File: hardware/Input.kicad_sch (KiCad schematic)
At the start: 40 parts, among them J10 USB_C_Receptacle_USB2.0, J4 AudioJack3, J5 Conn_Coaxial, J6 Conn_Coaxial, J7 Conn_Coaxial, J8 Conn_Coaxial, J9 Barrel_Jack_Switch, U23 74LVCH2T45DC, U24 74LVCH2T45DC, U25 74LVCH2T45DC

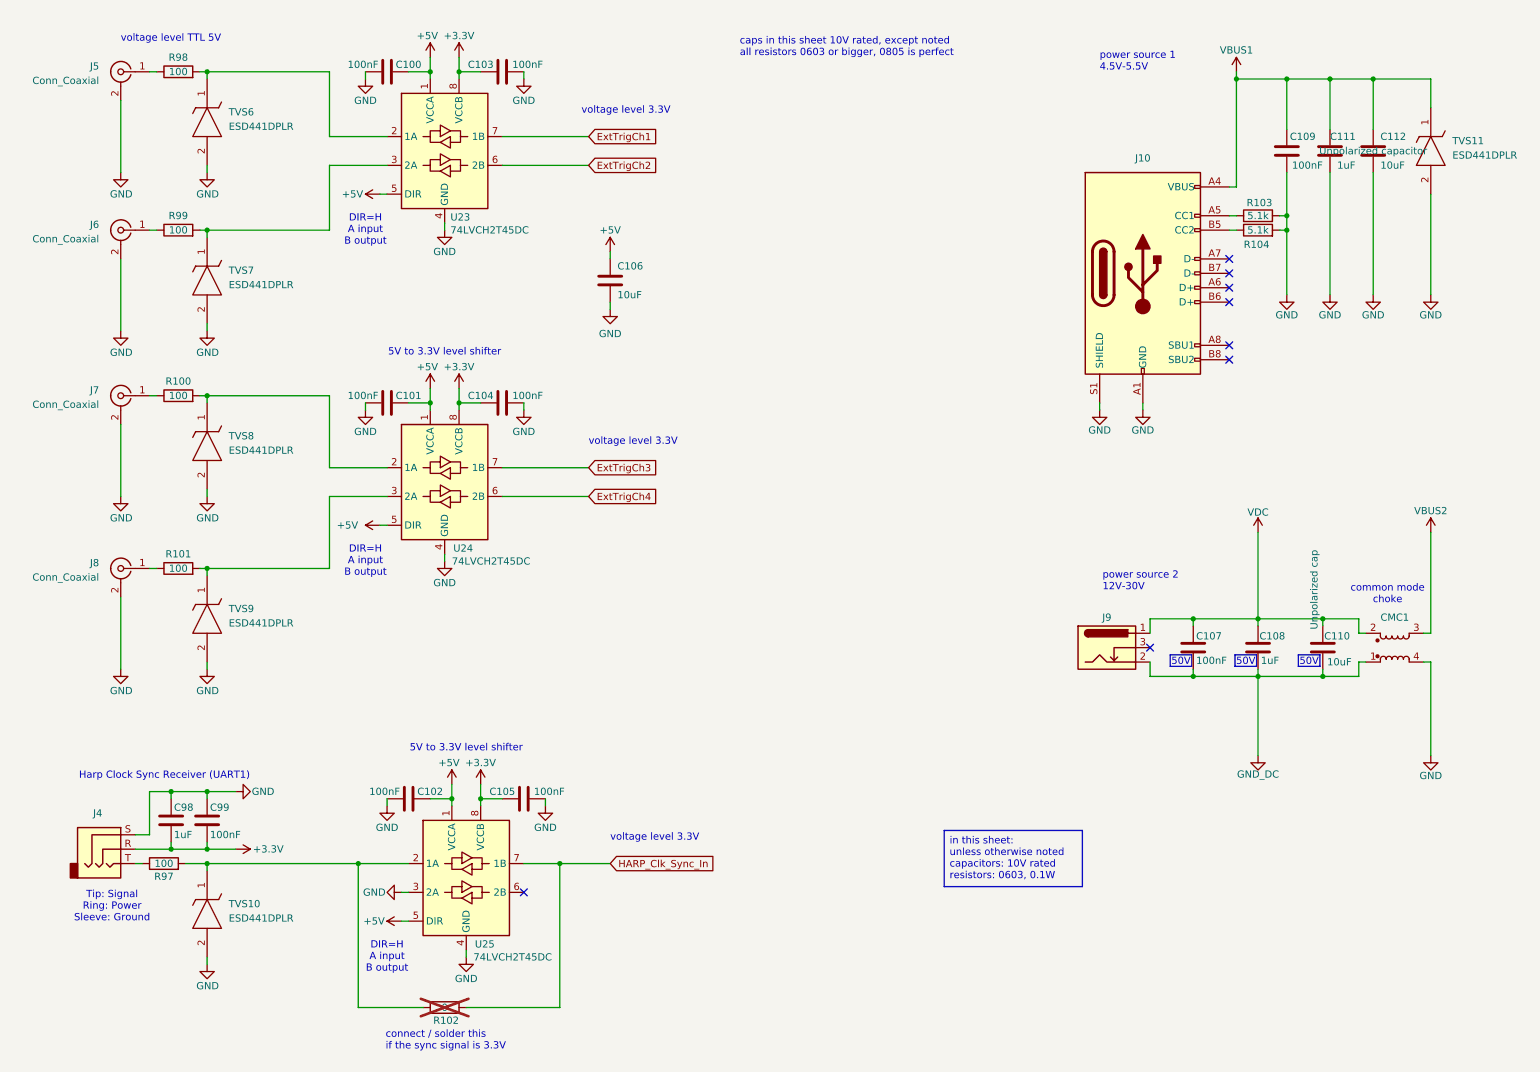
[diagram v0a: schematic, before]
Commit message: BOM for all capacitors and resistors is added correctly to the schematic
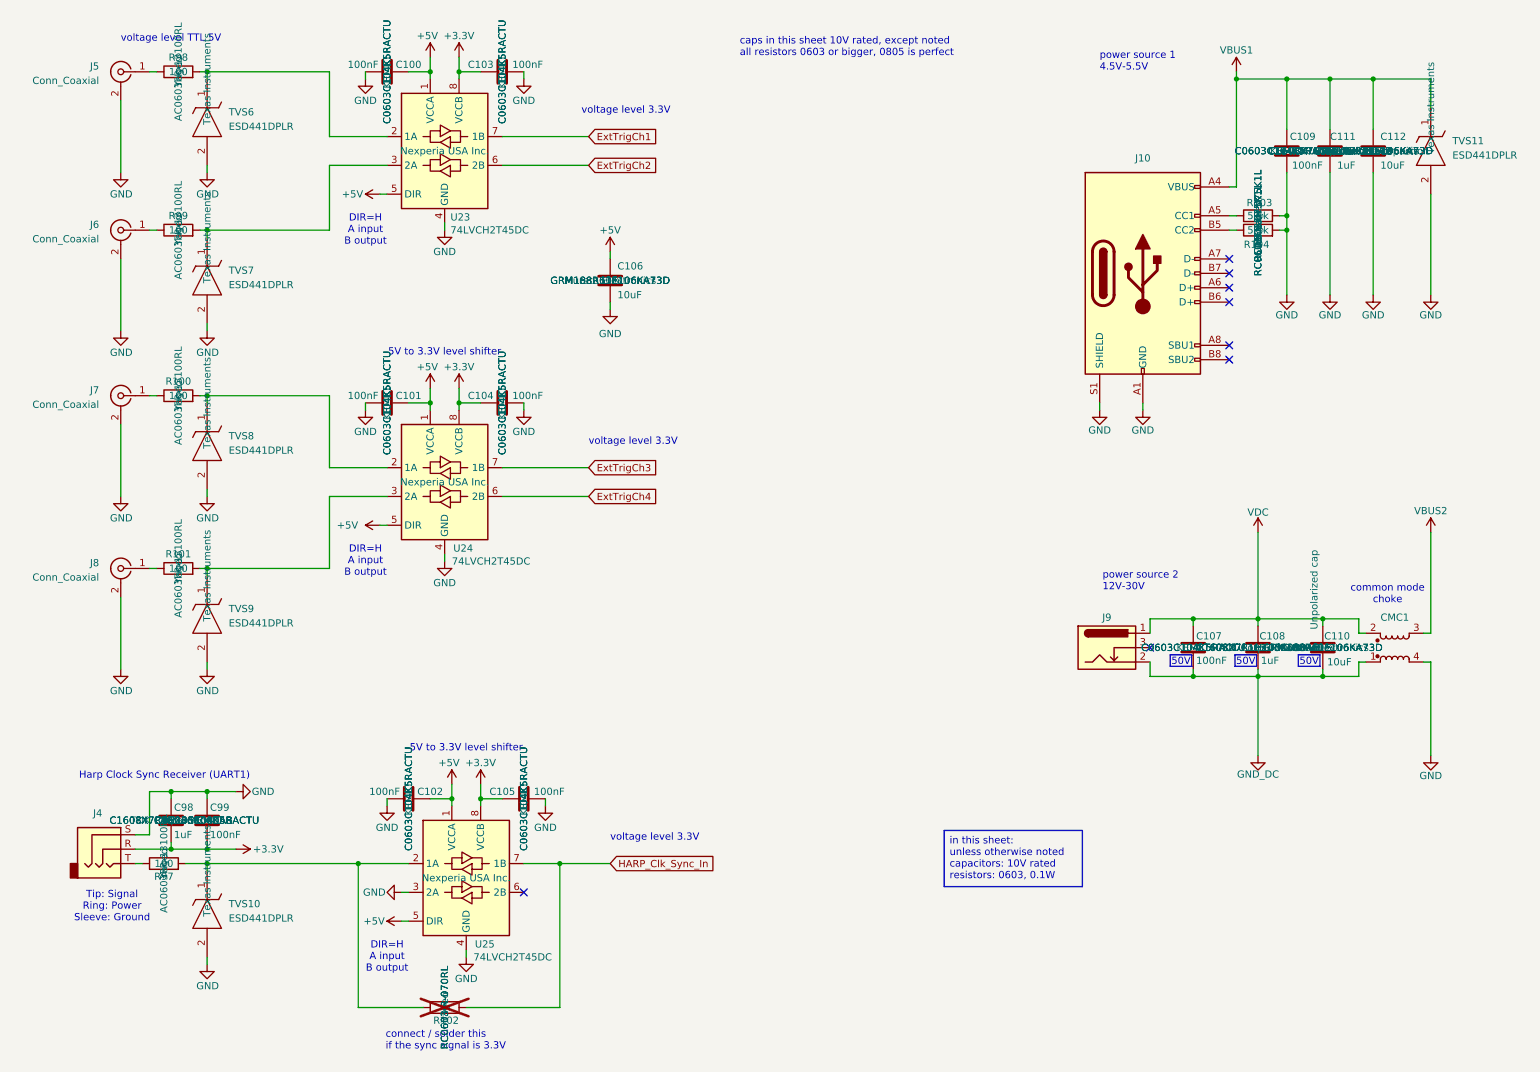
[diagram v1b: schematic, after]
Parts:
- C100, C101, C102, C103, C104, C105, C107, C109, C99: Link https://www.digikey.com/en/products/detail/walsin-technolog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 -> https://www.digikey.com/en/products/detail/kemet/C0603C104K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; MPN (none) -> C0603C104K5RACTU; Manufacturer Walson Technology Corporation -> KEMET; Manufacturer Number 0402B104K160CT -> (none); Manufacturer_Name (none) -> KEMET; Manufacturer_Part_Number (none) -> C0603C104K5RACTU; Rated Voltage 16V -> 50V
- C106, C110, C112: Link https://www.digikey.com/en/products/detail/murata-electronics/GRM21BZ71E106KE15L/13904911 -> https://www.digikey.com/en/products/detail/murata-electronics/GRM188R61E106KA73D/9867922; MPN (none) -> GRM188R61E106KA73D; Manufacturer Number GRM21BZ71E106KE15L -> (none); Manufacturer_Name (none) -> Murata Electronics; Manufacturer_Part_Number (none) -> GRM188R61E106KA73D; Tolerance (none) -> 10%
- C108, C111, C98: Link https://www.digikey.com/en/products/detail/murata-electroni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 -> https://www.digikey.com/en/products/detail/tdk-corporation/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; MPN (none) -> C1608X7R1H105K080AB; Manufacturer Murata Electronics -> TDK Corporation; Manufacturer Number GRM155R6YA105KE11J -> (none); Manufacturer_Name (none) -> TDK Corporation; Manufacturer_Part_Number (none) -> C1608X7R1H105K080AB; Rated Voltage 35V -> 50V; Tolerance (none) -> 10%
- CMC1: Link https://www.digikey.ca/en/products/detail/tdk-corporation/A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 -> (none)
- R100, R101, R97, R98, R99: Link https://www.digikey.com/en/products/detail/yageo/RT0402BRD0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 -> https://www.digikey.com/en/products/detail/yageo/AC0603FR-1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; MPN (none) -> AC0603FR-13100RL; Manufacturer_Name (none) -> Yageo; Manufacturer_Part_Number (none) -> AC0603FR-13100RL
- R102: Link https://www.digikey.com/en/products/detail/yageo/RT0402BRD0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 -> https://www.digikey.com/en/products/detail/yageo/RC0603JR-0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; MPN (none) -> RC0603JR-070RL; Manufacturer_Name (none) -> Yageo; Manufacturer_Part_Number (none) -> RC0603JR-070RL; Tolerance 1% -> (none)
- R103, R104: Link https://www.digikey.com/en/products/detail/yageo/RT0402FRE0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 -> https://www.digikey.com/en/products/detail/yageo/RC0603FR-0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; MPN (none) -> RC0603FR-075K1L; Manufacturer_Name (none) -> Yageo; Manufacturer_Part_Number (none) -> RC0603FR-075K1L
- TVS10, TVS11, TVS6, TVS7, TVS8, TVS9: Manufacturer (none) -> Texas Instruments
- U23, U24, U25: Manufacturer_Name (none) -> Nexperia USA Inc.

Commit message: Not necessary text is hidden + BOM on schematic
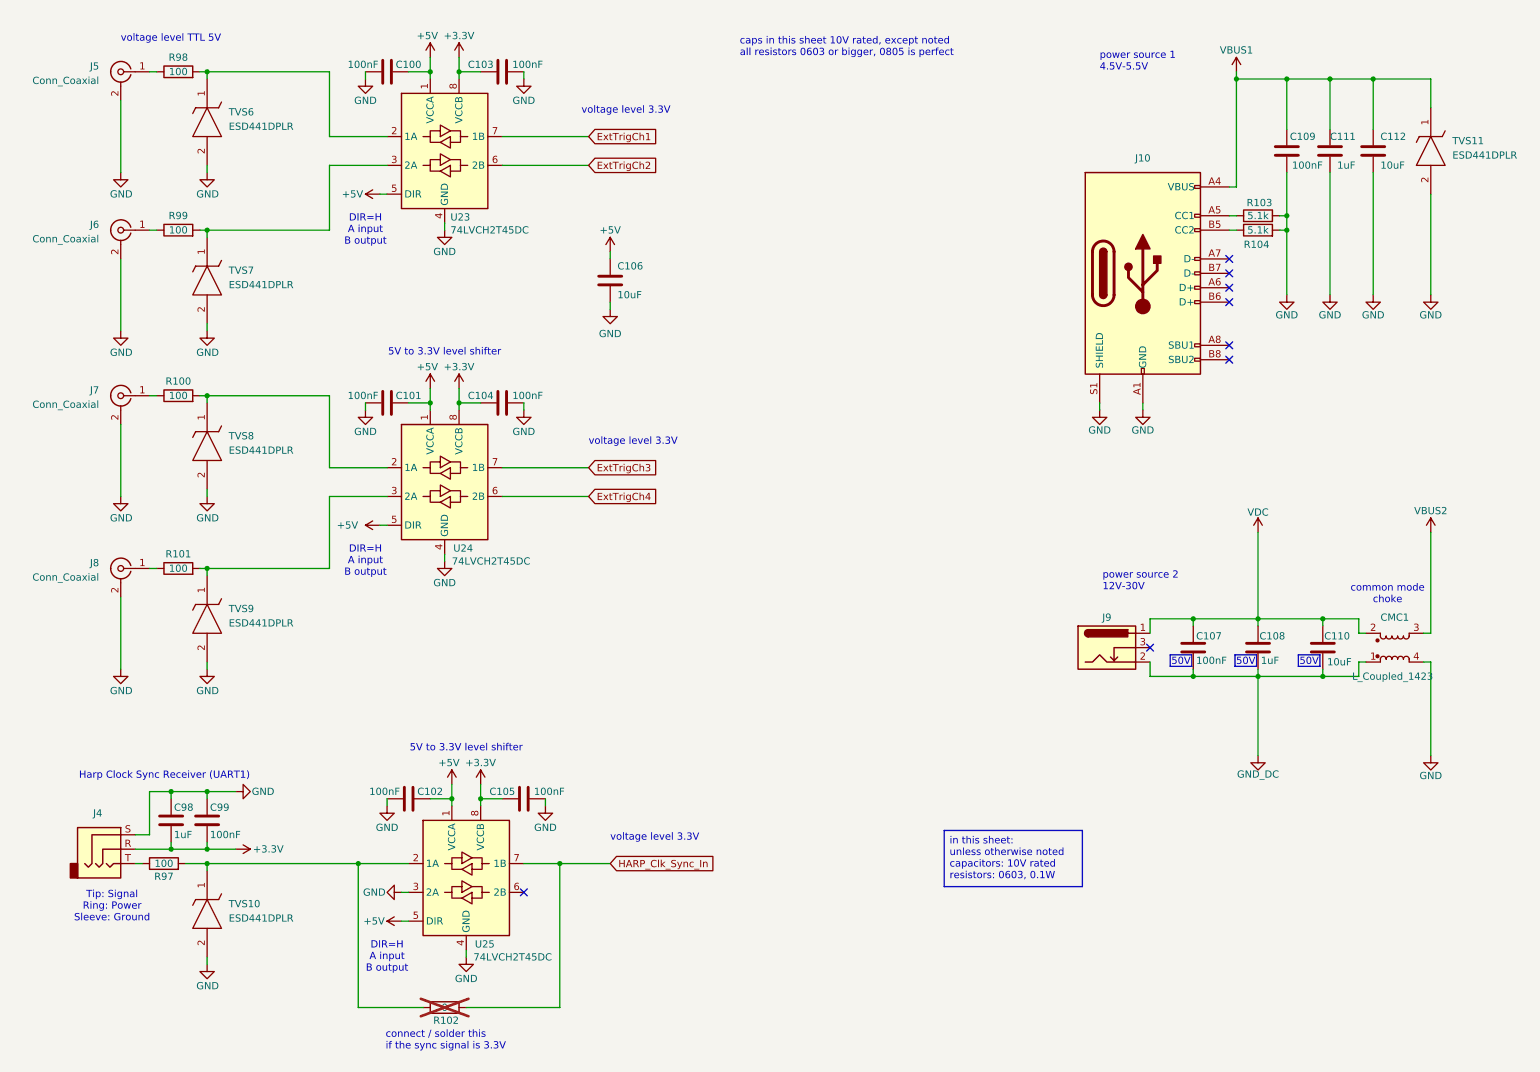
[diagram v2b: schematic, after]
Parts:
- C100, C101, C102, C103, C104, C105, C106, C107, C109, C110, C112, C99: Temperature Coefficient X7R -> (none)
- C108, C111, C98: Temperature Coefficient X5R -> (none)
- TVS10, TVS11, TVS6, TVS7, TVS8, TVS9: MPN (none) -> ESD441DPLR

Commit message: BOM cont.
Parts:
- J10: MPN (none) -> DX07S016JA1R1500; Manufacturer_Name (none) -> JAE Electronics; Manufacturer_Part_Number (none) -> DX07S016JA1R1500
- J4: MPN (none) -> SJ-3524-SMT-TR-BE; Manufacturer CUI Devices -> Same Sky (Formerly CUI Devices); Manufacturer_Name (none) -> Same Sky (Formerly CUI Devices); Manufacturer_Part_Number (none) -> SJ-3524-SMT-TR-BE
- J5, J6, J7, J8: Link (none) -> https://www.digikey.com/en/products/detail/te-connectivity-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; MPN (none) -> CONSMA002-SMD-G-T; Manufacturer (none) -> TE Connectivity Linx; Manufacturer_Name (none) -> TE Connectivity Linx; Manufacturer_Part_Number (none) -> CONSMA002-SMD-G-T
- J9: MPN (none) -> PJ-102AH; Manufacturer CUI Devices -> Same Sky (Formerly CUI Devices); Manufacturer_Name (none) -> Same Sky (Formerly CUI Devices); Manufacturer_Part_Number (none) -> PJ-102AH

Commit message: TVS16,TVS17,TVS18,TVS19 parts have been changed from ESDSB12VLB-TP to PESD12VL1BSLAZ
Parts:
- TVS10, TVS11, TVS6, TVS7, TVS8, TVS9: footprint ESD441DPLR -> harp.device.quad.dac.kicad:ESD441DPLR
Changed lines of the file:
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@@
 			)
 		)
-		(property "Footprint" "ESD441DPLR"
+		(property "Footprint" "harp.device.quad.dac.kicad:ESD441DPLR"
 			(at 50.8 90.17 0)
 			(effects
@@
 			)
 		)
-		(property "Footprint" "ESD441DPLR"
+		(property "Footprint" "harp.device.quad.dac.kicad:ESD441DPLR"
 			(at 50.8 33.02 0)
 			(effects
@@
 			)
 		)
-		(property "Footprint" "ESD441DPLR"
+		(property "Footprint" "harp.device.quad.dac.kicad:ESD441DPLR"
 			(at 266.7 38.1 0)
 			(effects
@@
 			)
 		)
-		(property "Footprint" "ESD441DPLR"
+		(property "Footprint" "harp.device.quad.dac.kicad:ESD441DPLR"
 			(at 50.8 172.72 0)
 			(effects
@@
 			)
 		)
-		(property "Footprint" "ESD441DPLR"
+		(property "Footprint" "harp.device.quad.dac.kicad:ESD441DPLR"
 			(at 50.8 60.96 0)
 			(effects
@@
 			)
 		)
-		(property "Footprint" "ESD441DPLR"
+		(property "Footprint" "harp.device.quad.dac.kicad:ESD441DPLR"
 			(at 50.8 120.65 0)
 			(effects

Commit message: The layout is complete, and the design is currently in the review stage.
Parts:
- J9: footprint Connector_BarrelJack:BarrelJack_CUI_PJ-102AH_Horizontal -> harp.device.quad.dac.kicad:BarrelJack_CUI_PJ-102AH_Horizontal
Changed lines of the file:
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@@
 			)
 		)
-		(property "Footprint" "Connector_BarrelJack:BarrelJack_CUI_PJ-102AH_Horizontal"
+		(property "Footprint" "harp.device.quad.dac.kicad:BarrelJack_CUI_PJ-102AH_Horizontal"
 			(at 207.01 124.206 0)
 			(effects

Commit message: Continue BOM + enhance BOM + enhance schematic
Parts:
- C108, C111, C98: Manufacturer TDK Corporation -> TDK; Manufacturer_Name TDK Corporation -> TDK
- CMC1: Link (none) -> https://www.digikey.com/en/products/detail/tdk-corporation/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; MPN (none) -> ACP3225-102-2P-T000; Manufacturer TDK Corporation -> TDK; Manufacturer_Name (none) -> TDK; Manufacturer_Part_Number (none) -> ACP3225-102-2P-T000
- TVS10, TVS11, TVS6, TVS7, TVS8, TVS9: Link (none) -> https://www.digikey.com/en/products/detail/texas-instrument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
- U23, U24, U25: MPN (none) -> 74LVCH2T45DC,125; Manufacturer Nexperia USA Inc. -> Nexperia; Manufacturer_Name Nexperia USA Inc. -> Nexperia; Manufacturer_Part_Number (none) -> 74LVCH2T45DC,125
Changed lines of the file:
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@@
 			)
 		)
-		(property "Manufacturer" "Nexperia USA Inc."
+		(property "Manufacturer" "Nexperia"
 			(at 88.9 35.56 0)
 			(effects
@@
 			)
 		)
-		(property "Manufacturer_Name" "Nexperia USA Inc."
+		(property "Manufacturer_Name" "Nexperia"
+			(at 88.9 35.56 0)
+			(effects
+				(font
+					(size 1.27 1.27)
+				)
+				(hide yes)
+			)
+		)
+		(property "MPN" "74LVCH2T45DC,125"
+			(at 88.9 35.56 0)
+			(effects
+				(font
+					(size 1.27 1.27)
+				)
+				(hide yes)
+			)
+		)
+		(property "Manufacturer_Part_Number" "74LVCH2T45DC,125"
 			(at 88.9 35.56 0)
 			(effects
@@
 			)
 		)
-		(property "Manufacturer" "TDK Corporation"
+		(property "Manufacturer" "TDK"
 			(at 40.64 153.67 0)
 			(effects
@@
 			)
 		)
-		(property "Manufacturer_Name" "TDK Corporation"
+		(property "Manufacturer_Name" "TDK"
 			(at 40.64 153.67 0)
 			(effects
@@
 			)
 		)
+		(property "Link" "https://www.digikey.com/en/products/detail/texas-instruments/ESD441DPLR/21298753"
+			(at 46.99 80.01 0)
+			(effects
+				(font
+					(size 1.27 1.27)
+				)
+				(hide yes)
+			)
+		)
 		(pin "2"
 		)
@@
 			)
 		)
-		(property "Manufacturer" "Nexperia USA Inc."
+		(property "Manufacturer" "Nexperia"
 			(at 92.71 163.83 0)
 			(effects
@@
 			)
 		)
-		(property "Manufacturer_Name" "Nexperia USA Inc."
+		(property "Manufacturer_Name" "Nexperia"
+			(at 92.71 163.83 0)
+			(effects
+				(font
+					(size 1.27 1.27)
+				)
+				(hide yes)
+			)
+		)
+		(property "MPN" "74LVCH2T45DC,125"
+			(at 92.71 163.83 0)
+			(effects
+				(font
+					(size 1.27 1.27)
+				)
+				(hide yes)
+			)
+		)
+		(property "Manufacturer_Part_Number" "74LVCH2T45DC,125"
 			(at 92.71 163.83 0)
 			(effects
@@
 			)
 		)
+		(property "Link" "https://www.digikey.com/en/products/detail/texas-instruments/ESD441DPLR/21298753"
+			(at 46.99 22.86 0)
+			(effects
+				(font
+					(size 1.27 1.27)
+				)
+				(hide yes)
+			)
+		)
 		(pin "2"
 		)
@@
 			)
 		)
-		(property "Link" ""
+		(property "Link" "https://www.digikey.com/en/products/detail/tdk-corporation/ACP3225-102-2P-T000/3024970"
 			(at 256.54 123.19 0)
 			(effects
@@
 			)
 		)
-		(property "Manufacturer" "TDK Corporation"
+		(property "Manufacturer" "TDK"
 			(at 256.54 123.19 0)
 			(effects
@@
 			)
 		)
+		(property "MPN" "ACP3225-102-2P-T000"
+			(at 256.54 123.19 0)
+			(effects
+				(font
+					(size 1.27 1.27)
+				)
+				(hide yes)
+			)
+		)
+		(property "Manufacturer_Name" "TDK"
+			(at 256.54 123.19 0)
+			(effects
+				(font
+					(size 1.27 1.27)
+				)
+				(hide yes)
+			)
+		)
+		(property "Manufacturer_Part_Number" "ACP3225-102-2P-T000"
+			(at 256.54 123.19 0)
+			(effects
+				(font
+					(size 1.27 1.27)
+				)
+				(hide yes)
+			)
+		)
 		(pin "1"
 		)
@@
 			)
 		)
+		(property "Link" "https://www.digikey.com/en/products/detail/texas-instruments/ESD441DPLR/21298753"
+			(at 262.89 27.94 0)
+			(effects
+				(font
+					(size 1.27 1.27)
+				)
+				(hide yes)
+			)
+		)
 		(pin "2"
 		)
@@
 			)
 		)
+		(property "Link" "https://www.digikey.com/en/products/detail/texas-instruments/ESD441DPLR/21298753"
+			(at 46.99 162.56 0)
+			(effects
+				(font
+					(size 1.27 1.27)
+				)
+				(hide yes)
+			)
+		)
 		(pin "2"
 		)
@@
 			)
 		)
-		(property "Manufacturer" "Nexperia USA Inc."
+		(property "Manufacturer" "Nexperia"
 			(at 88.9 93.98 0)
 			(effects
@@
 			)
 		)
-		(property "Manufacturer_Name" "Nexperia USA Inc."
+		(property "Manufacturer_Name" "Nexperia"
+			(at 88.9 93.98 0)
+			(effects
+				(font
+					(size 1.27 1.27)
+				)
+				(hide yes)
+			)
+		)
+		(property "MPN" "74LVCH2T45DC,125"
+			(at 88.9 93.98 0)
+			(effects
+				(font
+					(size 1.27 1.27)
+				)
+				(hide yes)
+			)
+		)
+		(property "Manufacturer_Part_Number" "74LVCH2T45DC,125"
 			(at 88.9 93.98 0)
 			(effects
@@
 			)
 		)
-		(property "Manufacturer" "TDK Corporation"
+		(property "Manufacturer" "TDK"
 			(at 245.11 35.56 0)
 			(effects
@@
 			)
 		)
-		(property "Manufacturer_Name" "TDK Corporation"
+		(property "Manufacturer_Name" "TDK"
 			(at 245.11 35.56 0)
 			(effects
@@
 			)
 		)
-		(property "Manufacturer" "TDK Corporation"
+		(property "Manufacturer" "TDK"
 			(at 232.41 123.19 0)
 			(effects
@@
 			)
 		)
-		(property "Manufacturer_Name" "TDK Corporation"
+		(property "Manufacturer_Name" "TDK"
 			(at 232.41 123.19 0)
 			(effects
@@
 			)
 		)
+		(property "Link" "https://www.digikey.com/en/products/detail/texas-instruments/ESD441DPLR/21298753"
+			(at 46.99 50.8 0)
+			(effects
+				(font
+					(size 1.27 1.27)
+				)
+				(hide yes)
+			)
+		)
 		(pin "2"
 		)
@@
 			(at 46.99 110.49 0)
 			(effects
+				(font
+					(size 1.27 1.27)
+				)
+				(hide yes)
+			)
+		)
+		(property "Link" "https://www.digikey.com/en/products/detail/texas-instruments/ESD441DPLR/21298753"
+			(at 46.99 110.49 0)
+			(effects

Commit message: The final review has been completed, and the manufacturing files have been generated.
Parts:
- C100, C101, C102, C103, C104, C105, C107, C109, C99: MPN C0603C104K5RACTU -> (none)
- C106, C110, C112: MPN GRM188R61E106KA73D -> (none)
- C108, C111, C98: MPN C1608X7R1H105K080AB -> (none)
- CMC1: MPN ACP3225-102-2P-T000 -> (none)
- J10: MPN DX07S016JA1R1500 -> (none)
- J4: MPN SJ-3524-SMT-TR-BE -> (none)
- J5, J6, J7, J8: MPN CONSMA002-SMD-G-T -> (none)
- J9: MPN PJ-102AH -> (none)
- R100, R101, R97, R98, R99: MPN AC0603FR-13100RL -> (none)
- R102: MPN RC0603JR-070RL -> (none)
- R103, R104: MPN RC0603FR-075K1L -> (none)
- TVS10, TVS11, TVS6, TVS7, TVS8, TVS9: MPN ESD441DPLR -> (none)
- U23, U24, U25: MPN 74LVCH2T45DC,125 -> (none)
